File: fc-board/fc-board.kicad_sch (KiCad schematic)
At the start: 7 parts, among them J1 ESQ-125-14-G-D, J2 MSXS-08PFFR-SF7002

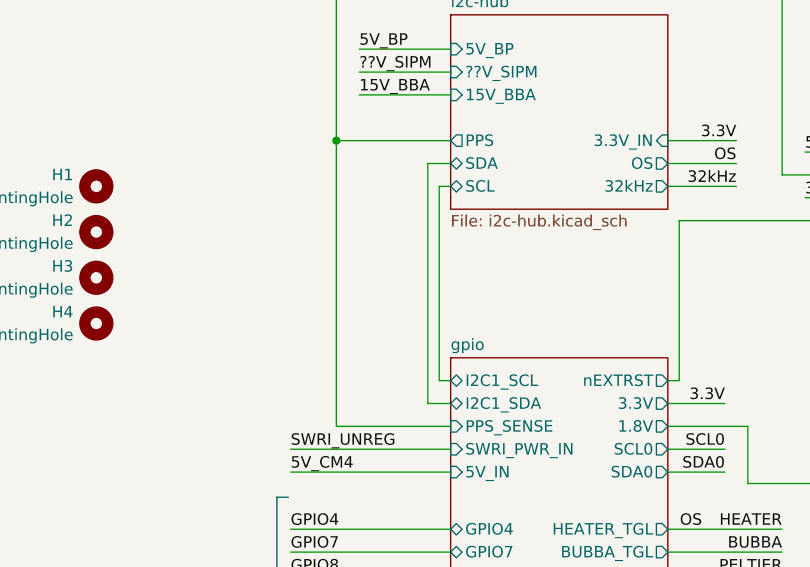
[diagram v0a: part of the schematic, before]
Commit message: Added test points to I2C lines
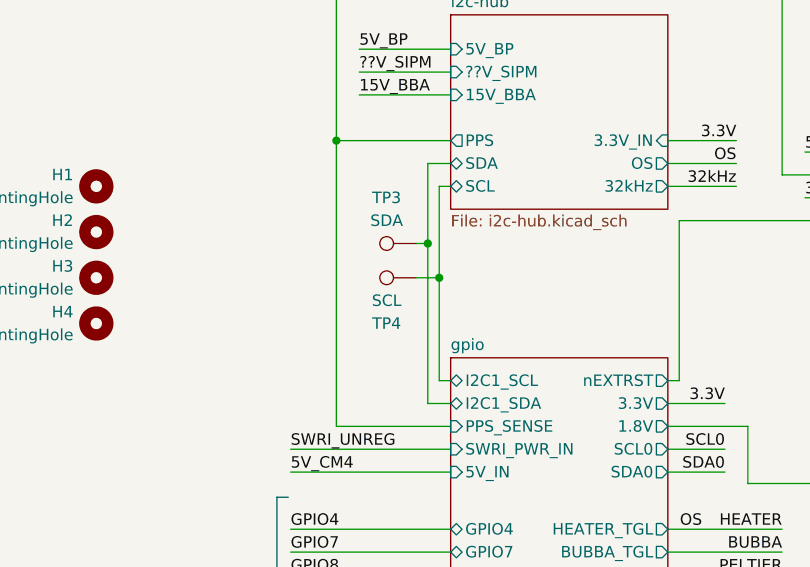
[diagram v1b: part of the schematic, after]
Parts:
- added TP3: SDA, fc-board:TestPoint_THTPad_D2.0mm_Drill1.0mm_JLCrules, symbol Connector:TestPoint
- added TP4: SCL, fc-board:TestPoint_THTPad_D2.0mm_Drill1.0mm_JLCrules, symbol Connector:TestPoint
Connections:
- net gpio/I2C1_SCL: now also TP4.1
- net gpio/I2C1_SDA: now also TP3.1
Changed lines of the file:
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@@
+	)
+	(junction
+		(at 106.68 58.42)
+		(diameter 0)
+		(color 0 0 0 0)
+	)
+	(junction
+		(at 105.41 54.61)
+		(diameter 0)
+		(color 0 0 0 0)
 	)
 	(junction
@@
 	(wire
 		(pts
+			(xy 105.41 54.61) (xy 105.41 72.39)
+		)
+		(stroke
+			(width 0)
+			(type default)
+		)
+	)
+	(wire
+		(pts
 			(xy 177.8 124.46) (xy 163.83 124.46)
 		)
@@
 	(wire
 		(pts
+			(xy 104.14 58.42) (xy 106.68 58.42)
+		)
+		(stroke
+			(width 0)
+			(type default)
+		)
+	)
+	(wire
+		(pts
 			(xy 167.64 111.76) (xy 177.8 111.76)
 		)
@@
 	(wire
 		(pts
+			(xy 104.14 54.61) (xy 105.41 54.61)
+		)
+		(stroke
+			(width 0)
+			(type default)
+		)
+	)
+	(wire
+		(pts
 			(xy 201.93 109.22) (xy 201.93 121.92)
 		)
@@
 	(wire
 		(pts
-			(xy 105.41 45.72) (xy 105.41 72.39)
+			(xy 105.41 45.72) (xy 105.41 54.61)
 		)
 		(stroke
@@
 	(wire
 		(pts
+			(xy 106.68 58.42) (xy 106.68 48.26)
+		)
+		(stroke
+			(width 0)
+			(type default)
+		)
+	)
+	(wire
+		(pts
 			(xy 132.08 91.44) (xy 144.78 91.44)
 		)
@@
 	(wire
 		(pts
-			(xy 106.68 69.85) (xy 106.68 48.26)
+			(xy 106.68 69.85) (xy 106.68 58.42)
 		)
 		(stroke
@@
 	)
 	(symbol
+		(lib_id "Connector:TestPoint")
+		(at 104.14 58.42 90)
+		(unit 1)
+		(exclude_from_sim no)
+		(in_bom yes)
+		(on_board yes)
+		(dnp no)
+		(property "Reference" "TP4"
+			(at 100.838 63.5 90)
+			(effects
+				(font
+					(size 1.27 1.27)
+				)
+			)
+		)
+		(property "Value" "SCL"
+			(at 100.838 60.96 90)
+			(effects
+				(font
+					(size 1.27 1.27)
+				)
+			)
+		)
+		(property "Footprint" "fc-board:TestPoint_THTPad_D2.0mm_Drill1.0mm_JLCrules"
+			(at 104.14 53.34 0)
+			(effects
+				(font
+					(size 1.27 1.27)
+				)
+				(hide yes)
+			)
+		)
+		(property "Datasheet" "~"
+			(at 104.14 53.34 0)
+			(effects
+				(font
+					(size 1.27 1.27)
+				)
+				(hide yes)
+			)
+		)
+		(property "Description" "test point"
+			(at 104.14 58.42 0)
+			(effects
+				(font
+					(size 1.27 1.27)
+				)
+				(hide yes)
+			)
+		)
+		(pin "1"
+		)
+		(instances
+			(project "fc-board"
+				(path "/14bbabed-904f-4efc-8ba4-be00e59385c4"
+					(reference "TP4")
+					(unit 1)
+				)
+			)
+		)
+	)
+	(symbol
 		(lib_id "power:GND")
 		(at 120.65 173.99 0)
@@
 					(unit 1)
 				)
+			)
+		)
+	)
+	(symbol
+		(lib_id "Connector:TestPoint")
+		(at 104.14 54.61 90)
+		(mirror x)
+		(unit 1)
+		(exclude_from_sim no)
+		(in_bom yes)
+		(on_board yes)
+		(dnp no)
+		(fields_autoplaced yes)
+		(property "Reference" "TP3"
+			(at 100.838 49.53 90)
+			(effects
+				(font
+					(size 1.27 1.27)
+				)
+			)
+		)
+		(property "Value" "SDA"
+			(at 100.838 52.07 90)
+			(effects
+				(font
+					(size 1.27 1.27)
+				)
+			)
+		)
+		(property "Footprint" "fc-board:TestPoint_THTPad_D2.0mm_Drill1.0mm_JLCrules"
+			(at 104.14 59.69 0)
+			(effects
+				(font
+					(size 1.27 1.27)
+				)
+				(hide yes)
+			)
+		)
+		(property "Datasheet" "~"
+			(at 104.14 59.69 0)
+			(effects
+				(font
+					(size 1.27 1.27)
+				)
+				(hide yes)
+			)
+		)
+		(property "Description" "test point"
+			(at 104.14 54.61 0)
+			(effects
+				(font
+					(size 1.27 1.27)
+				)
+				(hide yes)
+			)
+		)
+		(pin "1"
+		)
+		(instances
+			(project "fc-board"
+				(path "/14bbabed-904f-4efc-8ba4-be00e59385c4"
+					(reference "TP3")
+					(unit 1)
+				)

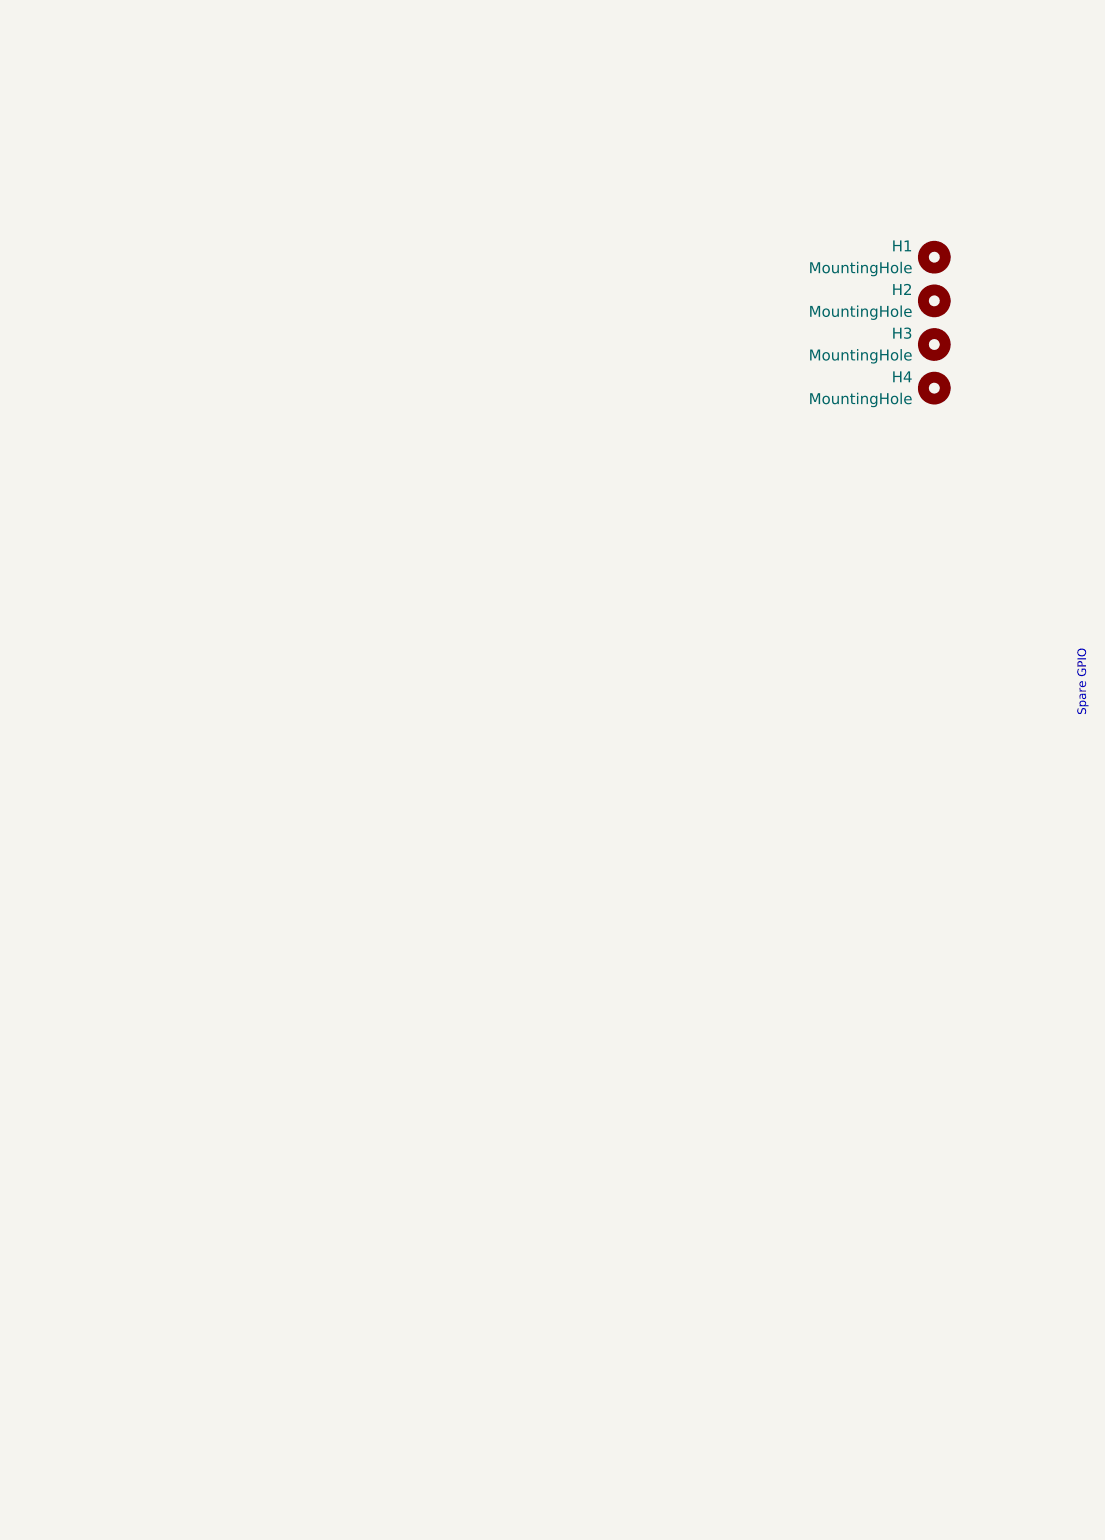
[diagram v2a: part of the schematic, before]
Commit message: Removed zips; updated gitignore
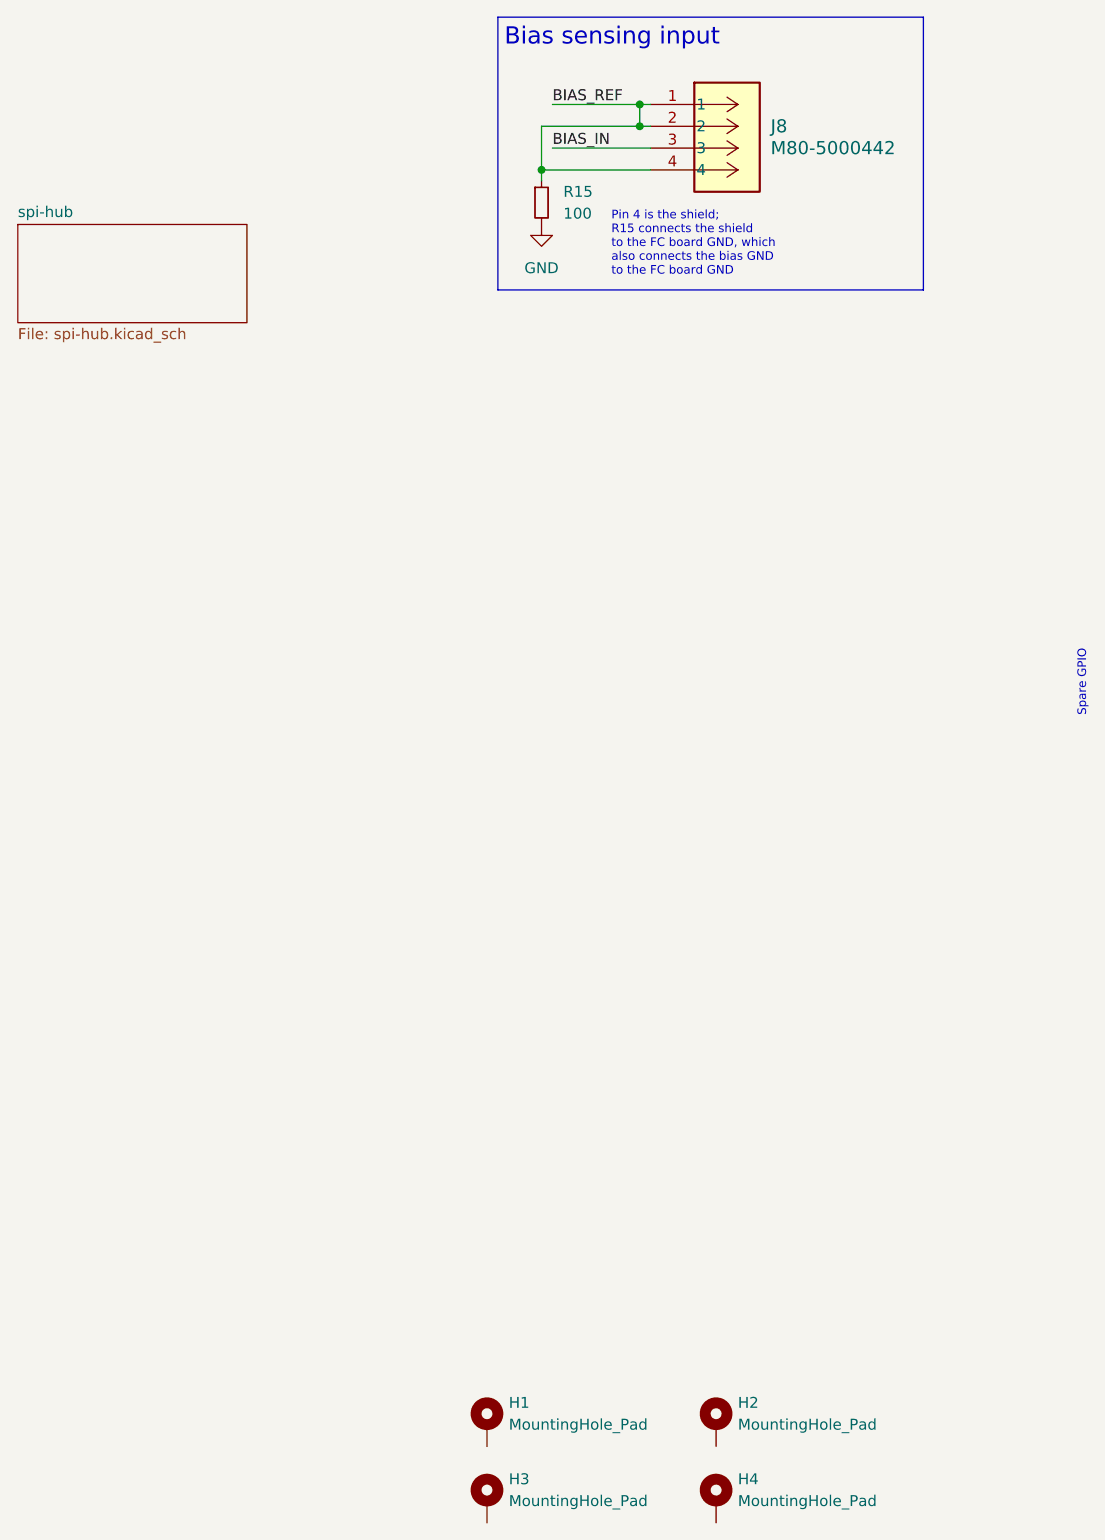
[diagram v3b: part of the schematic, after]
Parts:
- removed H1, H2, H3, H4: MountingHole, MountingHole:MountingHole_3.2mm_M3_Pad, symbol Mechanical:MountingHole
- added H1, H2, H3, H4: MountingHole_Pad, MountingHole:MountingHole_3.2mm_M3_Pad, symbol Mechanical:MountingHole_Pad
- added J8: M80-5000442, fc-board:M80_5000442, symbol fc-board:M80-5000442
- added R15: 100, Resistor_SMD:R_1206_3216Metric, symbol Device:R_Small
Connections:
- net GND: now also R15.2
- new net BIAS_IN: J8.3
- new net BIAS_REF: J8.1, J8.2, J8.4, R15.1
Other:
- added sheet spi-hub (spi-hub.kicad_sch)
- note added: "Bias sensing input"
- note added: "Pin 4 is the shield; R15 connects the shield to the FC board GND, which also connects the bias GND to the FC board GND"

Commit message: FC board updates
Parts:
- removed J1: ESQ-125-14-G-D, fc-board:ESQ-125-XX-X-D, symbol fc-board:ESQ-125-XX-X-D
- removed J2: MSXS-08PFFR-SF7002, fc-board:MSXS-08PFFR-SF7002, symbol fc-board:MSXS-08PFFR-SF7002
- removed JP14: P1 to GND, Jumper:SolderJumper-2_P1.3mm_Open_Pad1.0x1.5mm, symbol Jumper:SolderJumper_2_Open
- added J1: MSXS-08PFFR-SF7002, fc-board:MSXS-08PFFR-SF7002, symbol fc-board:MSXS-08PFFR-SF7002
- added J10: Conn_01x03_Pin, Connector_PinHeader_2.54mm:PinHeader_1x03_P2.54mm_Vertical, symbol Connector:Conn_01x03_Pin
- added J11: RJMG201K32630ER, fc-board:RJMG201K32630ER, symbol fc-board:RJMG201K32630ER
- added J2, J4, J5: M80-5000442, fc-board:M80_5000442, symbol fc-board:M80-5000442
- added J6: Conn_02x04_Counter_Clockwise, Connector_PinSocket_2.54mm:PinSocket_2x04_P2.54mm_Vertical, symbol Connector_Generic:Conn_02x04_Counter_Clockwise
- added J7: Conn_01x08_Pin, Connector_PinHeader_2.54mm:PinHeader_2x04_P2.54mm_Vertical, symbol Connector:Conn_01x08_Pin
- added J8: BCS-110-L-D-TE, fc-board:SAMTEC_BCS-110-L-D-TE, symbol fc-board:BCS-110-L-D-TE
- added J9: Conn_Coaxial_Small, Connector_Coaxial:MMCX_Molex_73415-1471_Vertical, symbol Connector:Conn_Coaxial_Small
- added JP1: P1 to GND, Jumper:SolderJumper-2_P1.3mm_Open_Pad1.0x1.5mm, symbol Jumper:SolderJumper_2_Open
- added R2, R3: 330, Resistor_SMD:R_1206_3216Metric, symbol Device:R_Small
- added TP1: SDA0, fc-board:TestPoint_THTPad_D2.0mm_Drill1.0mm_JLCrules, symbol Connector:TestPoint
- added TP2: SCL0, fc-board:TestPoint_THTPad_D2.0mm_Drill1.0mm_JLCrules, symbol Connector:TestPoint
- TP3: value SDA -> SDA1
- TP4: value SCL -> SCL1
- renumbered J8 to J3, R15 to R1
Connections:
- net 3.3V: now also J4.1, J5.1, R2.1, R3.1
- net GND: now also J4.2, J5.4, J7.2 (Pin_2), J7.4 (Pin_4), J7.6 (Pin_6), J8.15, J8.16, J8.17, J8.18, J8.19, J8.20, J9.2 (Ext), JP1.1 (A)
- net GPIO17: now also J7.1 (Pin_1)
- net GPIO18: now also J7.3 (Pin_3)
- net X1+: now also J2.1
- net X1-: now also J2.2
- net X2+: now also J2.3
- net X2-: now also J2.4
- net X3+: now also J1.3
- net X3-: now also J1.4
- net X4+: now also J1.1
- net X4-: now also J1.2
- net CHASSIS: now reaches H1.1
- net CHASSIS: now also H2.1, H3.1, H4.1
- new net: J11.L2, R3.2
- new net: J1.P1, JP1.2 (B)
- new net: J11.L1, R2.2
- new net +12V_HEAT: J6.4 (Pin_4)
- new net +15V_BBA: J6.6 (Pin_6)
- new net +5V_BP: J6.2 (Pin_2)
- new net +5V_CM4: J8.13, J8.14
- new net +5V_SIPM: J6.8 (Pin_8)
- new net +7.2V_CMT: J6.1 (Pin_1)
- new net -15V_BBA: J6.5 (Pin_5)
- new net -5V_SIPM: J6.3 (Pin_3)
- new net -7.2V_CMT: J6.7 (Pin_7)
- new net BUBBA_TGL: J8.11, J8.12
- new net DET1_TGL: J8.01, J8.02
- new net DET2_TGL: J8.03, J8.04
- new net DET3_TGL: J8.05, J8.06
- new net DET4_TGL: J8.07, J8.08
- new net GPIO19: J7.5 (Pin_5)
- new net GPIO20: J7.7 (Pin_7)
- new net GPIO21: J7.8 (Pin_8)
- new net HEATER_TGL: J8.09, J8.10
- new net I2C0_SCL: J4.4, TP2.1
- new net I2C0_SDA: J4.3, TP1.1
- new net PPS: J9.1 (In)
- new net SPI0_CLK: J10.1 (Pin_1)
- new net SPI0_MISO: J10.2 (Pin_2)
- new net SPI0_MOSI: J10.3 (Pin_3)
- new net UART_RX: J5.3
- new net UART_TX: J5.2
- new net Y1+: J11.P1 (TD1+)
- new net Y1-: J11.P2 (TD1-)
- new net Y2+: J11.P3 (TD2+)
- new net Y2-: J11.P4 (TD2-)
- new net Y3+: J11.P7 (TD3+)
- new net Y3-: J11.P8 (TD3-)
- new net Y4+: J11.P9 (TD4+)
- new net Y4-: J11.P10 (TD4-)
- no-connect marks 10 -> 0
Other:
- removed sheet usb-hub
- sheet gpio ports: added ETH_LEDG, ETH_LEDY1, GPIO19, GPIO20, GPIO21, I2C0_SCL, I2C0_SDA, SPI0_CE0, SPI0_CLK, SPI0_MISO, SPI0_MOSI, UART_RX, UART_TX; removed GPIO10, GPIO14, GPIO15, GPIO4, GPIO7, GPIO8, ID_SC, ID_SD, PELTIER_TGL, UPS_TGL
- sheet gpio-hispeed ports: added 3.3V, Y1+, Y1-, Y2+, Y2-, Y3+, Y3-, Y4+, Y4-, Y_DUPLEX_LED, Y_LINK_LED; removed USB2_N, USB2_P, USB_OTG_ID
- sheet i2c-hub ports: added +12V_HEAT, +15V_BBA, +5V_BP, +5V_CM4, +5V_IN, +5V_SIPM, +7V2_CMT, -15V_BBA, -5V_SIPM, -7V2_CMT, ADS_DRDY, ADS_RESET, BIAS_IN, BIAS_REF, RST; removed 15V_BBA, 5V_BP, ??V_SIPM
- sheet spi-hub ports: added CS_LTC2983, INTERRUPT_LTC2983, RESET_LTC2983, SCK, SDI, SDO; removed none
- note added: "3.3 V likely not needed, but included just in case."
- note added: "Bias I2C"
- note added: "Debug"
- note added: "Gondola ethernet"
- note added: "Interconnect to toggles board"
- note added: "NOT I2C"
- note added: "PULLUPS ON LEDS?"
- note added: "Pin 4 is the shield; R1 connects the shield to the FC board GND, which also connects the bias GND to the FC board GND"
- note added: "Voltage sensing inputs"
- note removed: "Add another 5 V pin to header?"
- note removed: "Interconnect to power board"
- note removed: "Pin 4 is the shield; R15 connects the shield to the FC board GND, which also connects the bias GND to the FC board GND"
- moved on the sheet: TP3, TP4

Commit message: Finished routing; cleaned library
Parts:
- removed J1: MSXS-08PFFR-SF7002, fc-board:MSXS-08PFFR-SF7002, symbol fc-board:MSXS-08PFFR-SF7002
- added C1, C2: 0.1u, Capacitor_SMD:C_0805_2012Metric, symbol Device:C_Small
- added J4: M80-5000442, fc-board:M80_5000442, symbol fc-board:M80-5000442
- added J7: Conn_02x02_Counter_Clockwise, Connector_PinHeader_2.54mm:PinHeader_2x02_P2.54mm_Vertical, symbol Connector_Generic:Conn_02x02_Counter_Clockwise
- added J9: Conn_01x02_Pin, Connector_PinHeader_2.54mm:PinHeader_1x02_P2.54mm_Vertical, symbol Connector:Conn_01x02_Pin
- added JP2: SHIELD, Resistor_SMD:R_1206_3216Metric_Pad1.30x1.75mm_HandSolder, symbol Jumper:SolderJumper_2_Open
- added JP3: SHIELD1, Resistor_SMD:R_1206_3216Metric_Pad1.30x1.75mm_HandSolder, symbol Jumper:SolderJumper_2_Open
- added TP10: Global_EN, fc-board:TestPoint_THTPad_D2.0mm_Drill1.0mm_JLCrules, symbol Connector:TestPoint
- added TP5: +5V, fc-board:TestPoint_THTPad_D2.0mm_Drill1.0mm_JLCrules, symbol Connector:TestPoint
- added TP6: ADS_DRDY, fc-board:TestPoint_THTPad_D2.0mm_Drill1.0mm_JLCrules, symbol Connector:TestPoint
- added TP7: nEXTRST, fc-board:TestPoint_THTPad_D2.0mm_Drill1.0mm_JLCrules, symbol Connector:TestPoint
- added TP8: TestPoint, fc-board:TestPoint_THTPad_D2.0mm_Drill1.0mm_JLCrules, symbol Connector:TestPoint
- added TP9: +3V3, fc-board:TestPoint_THTPad_D2.0mm_Drill1.0mm_JLCrules, symbol Connector:TestPoint
- J12: renamed from J10; now not fitted
- JP1: value P1 to GND -> nRPIBOOT
- renumbered J2 to J1, J8 to J10, J9 to J11, J11 to J13, J3 to J2, J4 to J3, J7 to J8
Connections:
- net GPIO21 is gone; now on net GND: J8.8 (Pin_8)
- net +5V_CM4: now also J7.1 (Pin_1), TP5.1
- net 3.3V: now also J4.1, TP9.1
- net GND: now also J5.2, JP1.2 (B), C1.1, C2.1, J4.2, J7.2 (Pin_2), JP2.2 (B), JP3.2 (B); no longer J5.4, JP1.1 (A)
- net GPIO19: now also J8.7 (Pin_7); no longer J8.5 (Pin_5)
- net GPIO20: now also J8.5 (Pin_5); no longer J8.7 (Pin_7)
- net SCL0: now also J9.2 (Pin_2)
- net SDA0: now also J9.1 (Pin_1)
- net UART_TX: now also J5.4; no longer J5.2
- net X1+: now also J1.3; no longer J1.1
- net X1-: now also J1.1; no longer J1.2
- net X2+: now also J1.4; no longer J1.3
- net X2-: now also J1.2; no longer J1.4
- net gpio/nEXTRST: now also TP7.1
- net i2c-hub/ADS_DRDY: now also TP6.1
- net i2c-hub/ADS_RESET: now also TP8.1
- net nRPIBOOT: now also JP1.1 (A)
- net at R3.2: now also J13.L3; no longer J13.L2
- net Y_DUPLEX_LED: now reaches J13.L4
- net at J13.P5 (TCT): now also C1.2
- net at J13.P6 (TCT__1): now also C2.2
- net at J13.SH1 (SHIELD): now also JP2.1 (A)
- net at J13.SH2 (SHIELD__1): now also JP3.1 (A)
- removed net CHASSIS: H1.1, H2.1, H3.1, H4.1
- net gpio/I2C1_SCL renamed I2C1_SCL
- net I2C1_SCL: now also J4.4
- net gpio/I2C1_SDA renamed I2C1_SDA
- net I2C1_SDA: now also J4.3
- new net USB_N: J7.3 (Pin_3)
- new net USB_P: J7.4 (Pin_4)
- new net Y_LINK_LED: J13.L2
- new net gpio/Global_EN: TP10.1
- no-connect marks 0 -> 6
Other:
- sheet gpio ports: added none; removed SWRI_PWR_IN, X3+, X3-, X4+, X4-
- sheet gpio-hispeed ports: added USB_N, USB_P; removed none
- sheet i2c-hub ports: added BIAS_SCL, BIAS_SDA; removed none
- sheet spi-hub ports: added 3.3V; removed none
- note added: "Can be repurposed to an additional I2C bus"
- note added: "General I2C"
- note added: "Jumpers for connecting shield to GND with either resistor or capacitor"
- note added: "NOT I2C But can be repurposed"
- note added: "Pull low to boot from USB"
- note added: "SDA0/SCL0"
- note added: "The LAN7430 PCIE card shows capacitors connecting the center taps to GND"
- note added: "USB"
- note added: "Unsure if the LEDs are properly labeled on the symbol; don't have a part in house to check atm."
- note removed: "NOT I2C"
- note removed: "PULLUPS ON LEDS?"
- title: (none) -> Flight Computer Carrier
- moved on the sheet: H1, H2, H3, H4, J1, J13, J5, J6, J8, R2, R3, TP1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
